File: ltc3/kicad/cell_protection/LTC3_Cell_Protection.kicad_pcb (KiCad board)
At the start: 4 copper layers, 92.2 x 67.1 mm, 77 parts, among them P1 S2BPHKS, P2 PIN_HEAD_1x2, P3 MicroFit header, P4 XH header, straight, P7 MicroFit head., P8 MicroFit head., P9 XH header, straight, Q1 SUM110P08-11, Q2 SUM110P08-11, Q3 NDS9407, Q4 SUM110P08-11, Q5 SUM110P08-11, Q6 MMBT3904, U1 BQ77PL900, U2 LTC2990

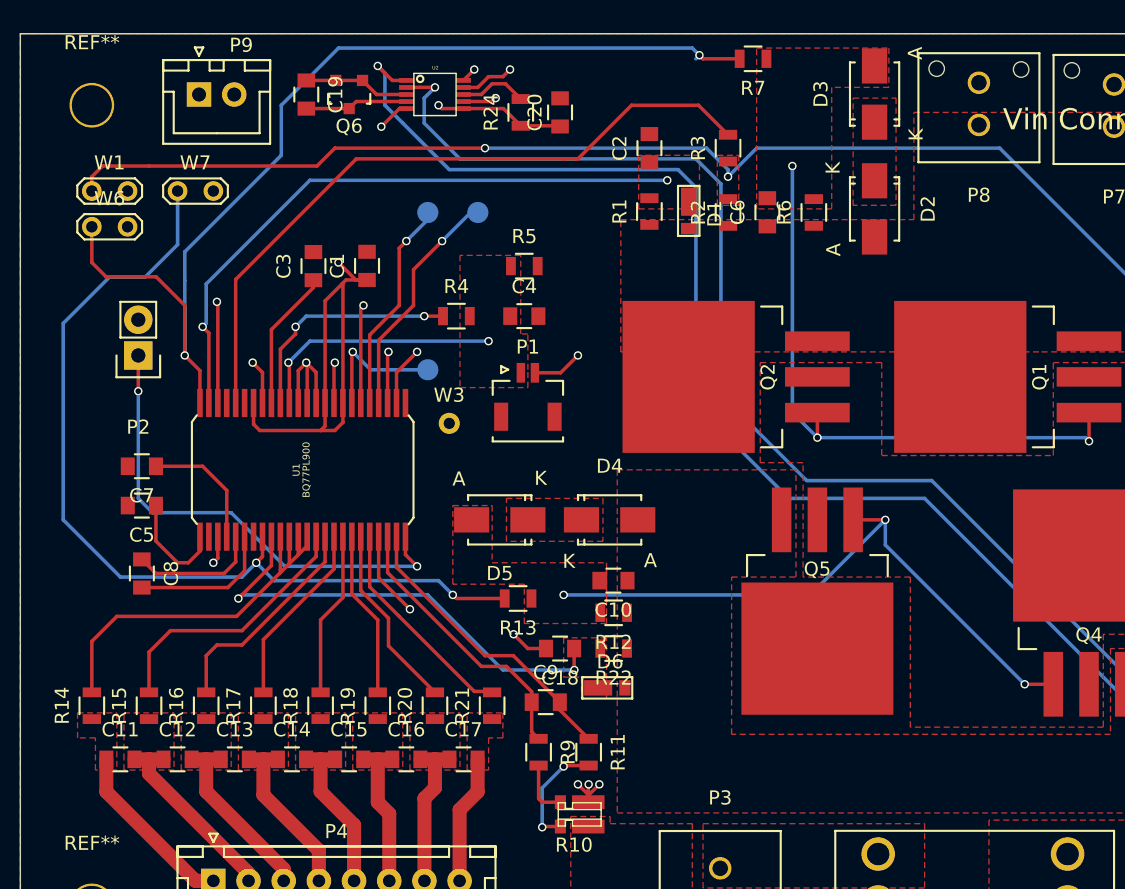
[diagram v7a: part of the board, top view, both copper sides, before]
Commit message: LTC3: Layout
Moved silk screen references so they are visible.
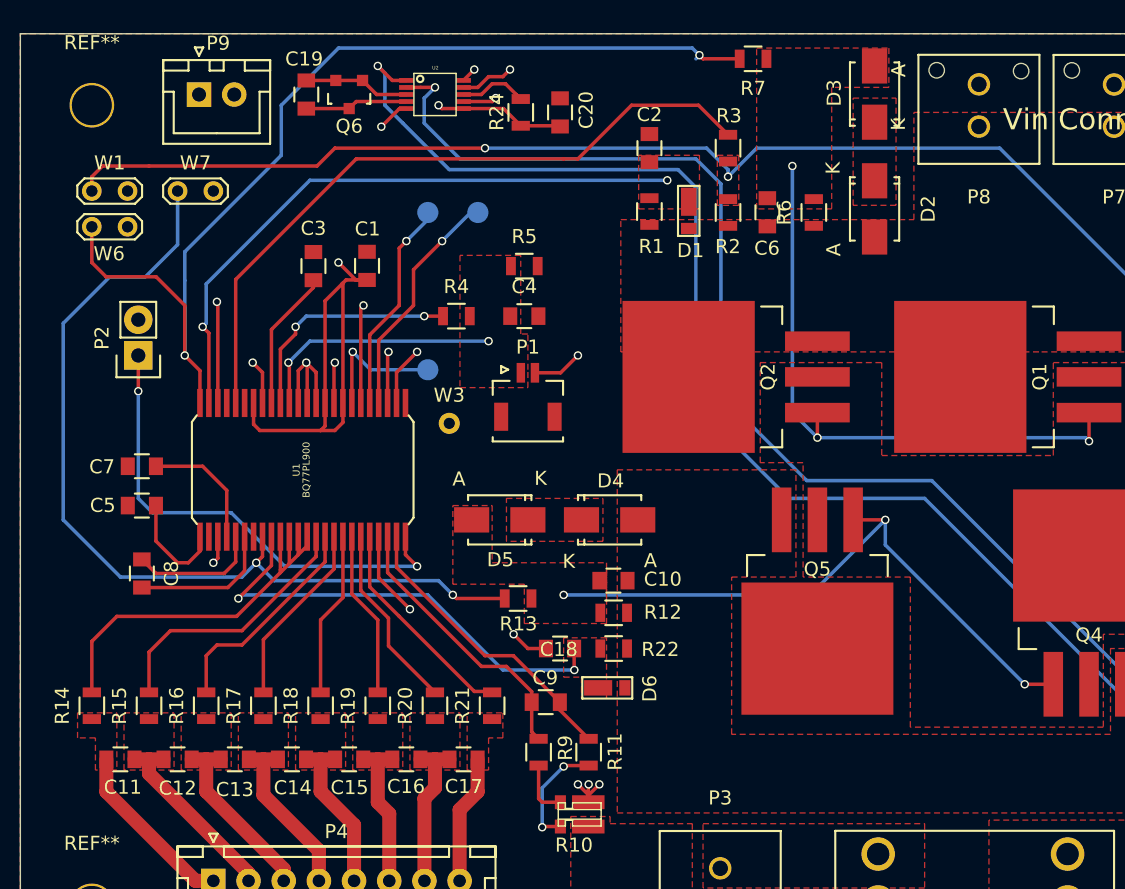
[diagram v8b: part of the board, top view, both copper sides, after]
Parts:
- moved P8 0.11 mm to (171.8, 73.1)
